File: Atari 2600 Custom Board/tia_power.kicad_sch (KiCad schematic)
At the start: 28 parts, among them J3 USB_C_Receptacle_PowerOnly_6P, Q1 2N3906, SW7 Power, Y1 3.579545 MHz

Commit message: Cleaned up electrical rules violations
Cleaned up electrical rules violations
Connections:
- net CLOCK_IN renamed PHI_2
- net CLOCK_OUT renamed PHI_0
- net ~{RDY} renamed READY
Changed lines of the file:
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@@
 	)
 	(junction
+		(at 76.2 151.13)
+		(diameter 0)
+		(color 0 0 0 0)
+	)
+	(junction
 		(at 228.6 57.15)
 		(diameter 0)
@@
 	)
 	(junction
+		(at 36.83 182.88)
+		(diameter 0)
+		(color 0 0 0 0)
+	)
+	(junction
 		(at 157.48 100.33)
 		(diameter 0)
@@
 	(wire
 		(pts
+			(xy 76.2 151.13) (xy 76.2 157.48)
+		)
+		(stroke
+			(width 0)
+			(type default)
+		)
+	)
+	(wire
+		(pts
 			(xy 55.88 48.26) (xy 55.88 58.42)
 		)
@@
 	(wire
 		(pts
-			(xy 76.2 148.59) (xy 76.2 157.48)
+			(xy 76.2 148.59) (xy 76.2 151.13)
 		)
 		(stroke
@@
 		)
 	)
-	(global_label "CLOCK_OUT"
-		(shape input)
+	(global_label "PHI_0"
+		(shape output)
 		(at 152.4 59.69 180)
 		(fields_autoplaced yes)
@@
 		)
 		(property "Intersheetrefs" "${INTERSHEET_REFS}"
-			(at 138.65 59.69 0)
+			(at 144.0324 59.69 0)
 			(effects
 				(font
@@
 		)
 	)
-	(global_label "CLOCK_IN"
-		(shape output)
+	(global_label "PHI_2"
+		(shape input)
 		(at 204.47 87.63 0)
 		(fields_autoplaced yes)
@@
 		)
 		(property "Intersheetrefs" "${INTERSHEET_REFS}"
-			(at 216.5267 87.63 0)
+			(at 212.8376 87.63 0)
 			(effects
 				(font
@@
 		)
 	)
-	(global_label "~{RDY}"
+	(global_label "READY"
 		(shape output)
 		(at 135.89 57.15 180)
@@
 		)
 		(property "Intersheetrefs" "${INTERSHEET_REFS}"
-			(at 129.2762 57.15 0)
+			(at 127.0386 57.15 0)
 			(effects
 				(font
@@
 	)
 	(symbol
+		(lib_id "power:PWR_FLAG")
+		(at 102.87 152.4 270)
+		(unit 1)
+		(exclude_from_sim no)
+		(in_bom yes)
+		(on_board yes)
+		(dnp no)
+		(fields_autoplaced yes)
+		(property "Reference" "#FLG01"
+			(at 104.775 152.4 0)
+			(effects
+				(font
+					(size 1.27 1.27)
+				)
+				(hide yes)
+			)
+		)
+		(property "Value" "PWR_FLAG"
+			(at 106.68 152.3999 90)
+			(effects
+				(font
+					(size 1.27 1.27)
+				)
+				(justify left)
+			)
+		)
+		(property "Footprint" ""
+			(at 102.87 152.4 0)
+			(effects
+				(font
+					(size 1.27 1.27)
+				)
+				(hide yes)
+			)
+		)
+		(property "Datasheet" "~"
+			(at 102.87 152.4 0)
+			(effects
+				(font
+					(size 1.27 1.27)
+				)
+				(hide yes)
+			)
+		)
+		(property "Description" "Special symbol for telling ERC where power comes from"
+			(at 102.87 152.4 0)
+			(effects
+				(font
+					(size 1.27 1.27)
+				)
+				(hide yes)
+			)
+		)
+		(pin "1"
+		)
+		(instances
+			(project "atari2600"
+				(path "/d26a1e82-f8cb-48a3-8cce-edbb66ba228a/1512de0d-3d07-49f3-86b5-e084744fd125"
+					(reference "#FLG01")
+					(unit 1)
+				)
+			)
+		)
+	)
+	(symbol
 		(lib_id "Device:C")
 		(at 217.17 41.91 180)
@@
 					(unit 1)
 				)
+			)
+		)
+	)
+	(symbol
+		(lib_id "power:PWR_FLAG")
+		(at 76.2 151.13 90)
+		(unit 1)
+		(exclude_from_sim no)
+		(in_bom yes)
+		(on_board yes)
+		(dnp no)
+		(fields_autoplaced yes)
+		(property "Reference" "#FLG02"
+			(at 74.295 151.13 0)
+			(effects
+				(font
+					(size 1.27 1.27)
+				)
+				(hide yes)
+			)
+		)
+		(property "Value" "PWR_FLAG"
+			(at 72.39 151.1299 90)
+			(effects
+				(font
+					(size 1.27 1.27)
+				)
+				(justify left)
+			)
+		)
+		(property "Footprint" ""
+			(at 76.2 151.13 0)
+			(effects
+				(font
+					(size 1.27 1.27)
+				)
+				(hide yes)
+			)
+		)
+		(property "Datasheet" "~"
+			(at 76.2 151.13 0)
+			(effects
+				(font
+					(size 1.27 1.27)
+				)
+				(hide yes)
+			)
+		)
+		(property "Description" "Special symbol for telling ERC where power comes from"
+			(at 76.2 151.13 0)
+			(effects
+				(font
+					(size 1.27 1.27)
+				)
+				(hide yes)
+			)
+		)
+		(pin "1"
+		)
+		(instances
+			(project "atari2600"
+				(path "/d26a1e82-f8cb-48a3-8cce-edbb66ba228a/1512de0d-3d07-49f3-86b5-e084744fd125"
+					(reference "#FLG02")
+					(unit 1)
+				)
+			)
+		)
+	)
+	(symbol
+		(lib_id "power:PWR_FLAG")
+		(at 36.83 182.88 270)
+		(unit 1)
+		(exclude_from_sim no)
+		(in_bom yes)
+		(on_board yes)
+		(dnp no)
+		(fields_autoplaced yes)
+		(property "Reference" "#FLG03"
+			(at 38.735 182.88 0)
+			(effects
+				(font
+					(size 1.27 1.27)
+				)
+				(hide yes)
+			)
+		)
+		(property "Value" "PWR_FLAG"
+			(at 40.64 182.8799 90)
+			(effects
+				(font
+					(size 1.27 1.27)
+				)
+				(justify left)
+			)
+		)
+		(property "Footprint" ""
+			(at 36.83 182.88 0)
+			(effects
+				(font
+					(size 1.27 1.27)
+				)
+				(hide yes)
+			)
+		)
+		(property "Datasheet" "~"
+			(at 36.83 182.88 0)
+			(effects
+				(font
+					(size 1.27 1.27)
+				)
+				(hide yes)
+			)
+		)
+		(property "Description" "Special symbol for telling ERC where power comes from"
+			(at 36.83 182.88 0)
+			(effects
+				(font
+					(size 1.27 1.27)
+				)
+				(hide yes)
+			)
+		)
+		(pin "1"
+		)
+		(instances
+			(project "atari2600"
+				(path "/d26a1e82-f8cb-48a3-8cce-edbb66ba228a/1512de0d-3d07-49f3-86b5-e084744fd125"
+					(reference "#FLG03")
+					(unit 1)
+				)

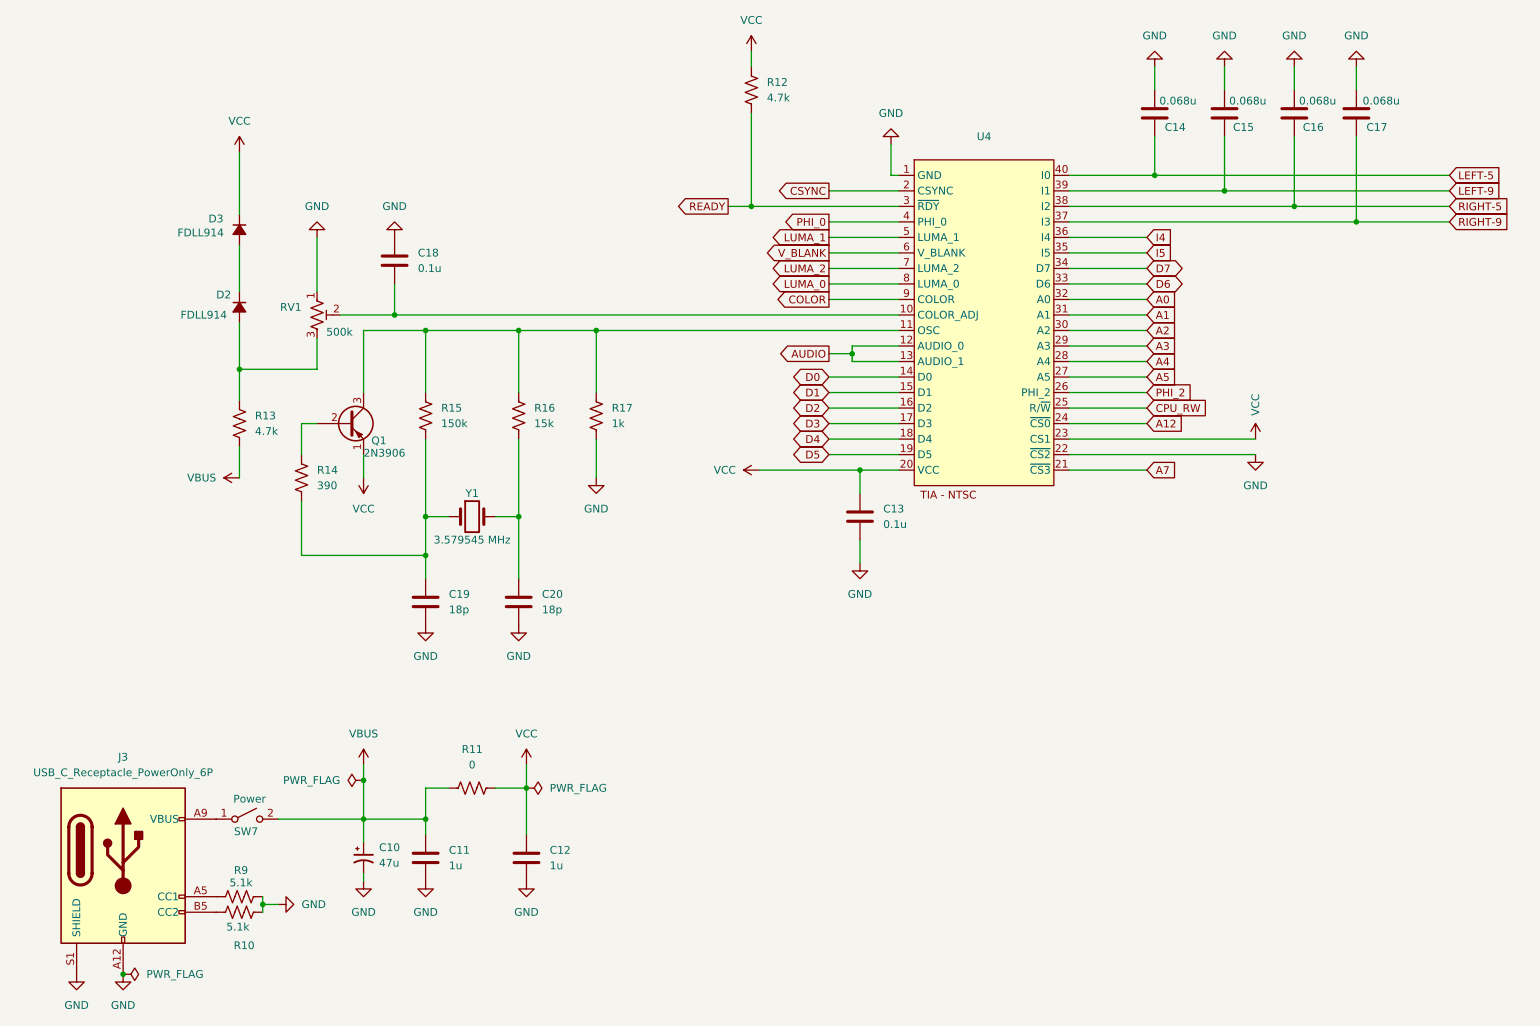
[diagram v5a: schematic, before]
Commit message: Fixed some incorrect values and re-annotated
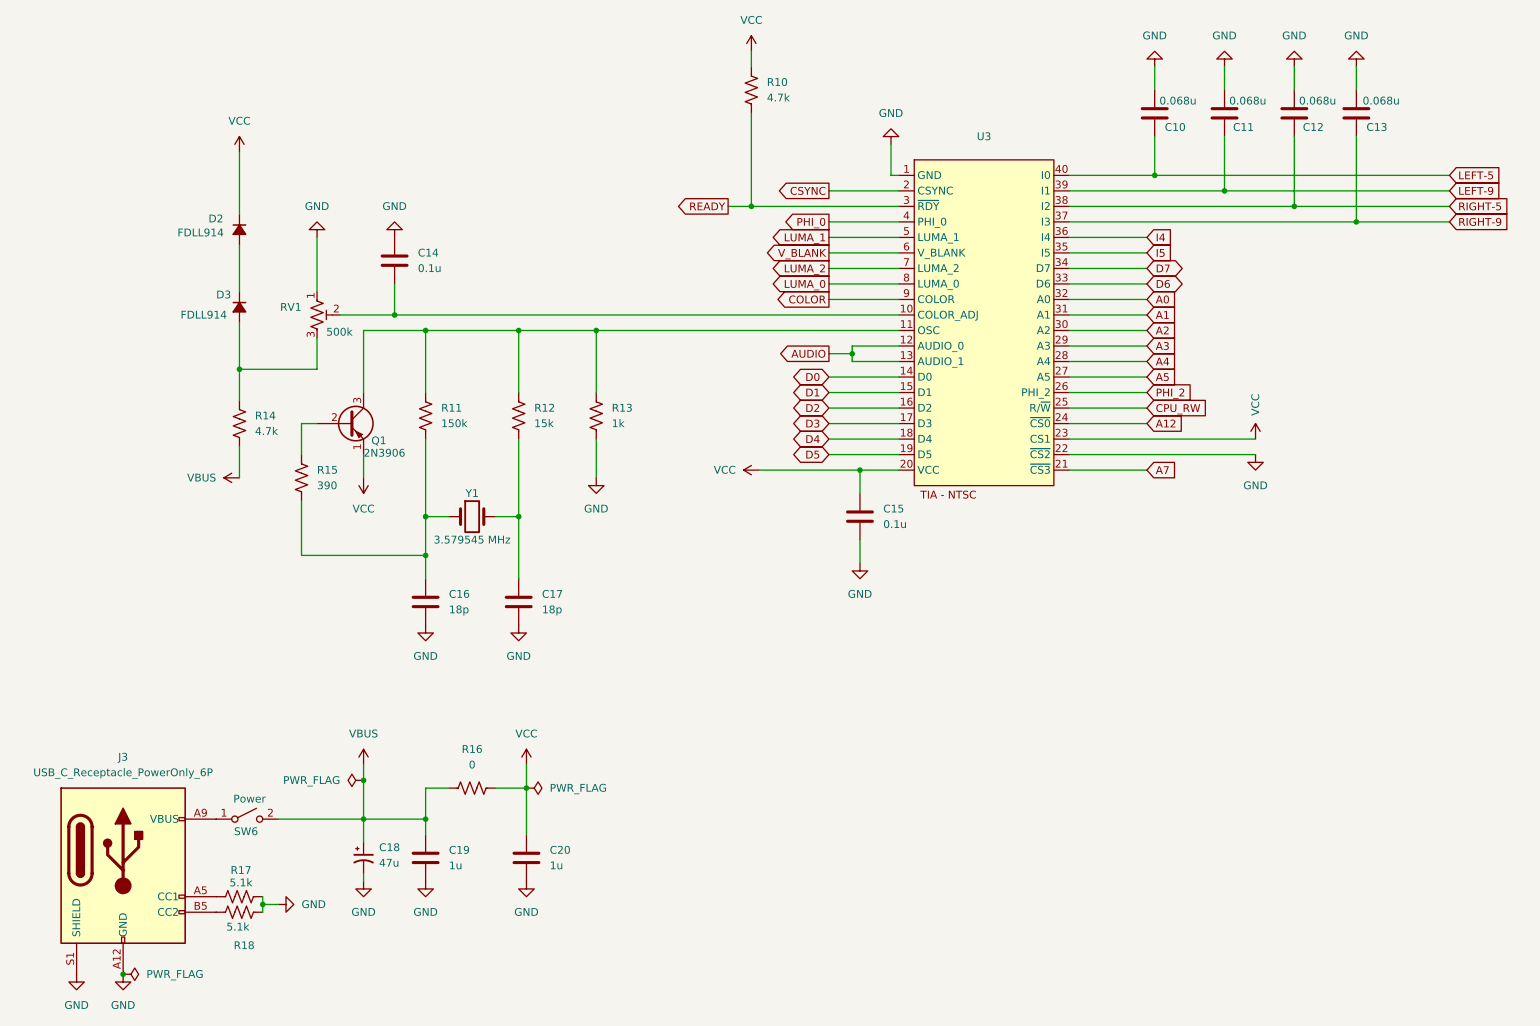
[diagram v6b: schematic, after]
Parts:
- renumbered C14 to C10, C15 to C11, C16 to C12, C17 to C13, C18 to C14, C13 to C15, C19 to C16, C20 to C17, C10 to C18, C11 to C19, C12 to C20, D3 to D2, D2 to D3, R12 to R10, R15 to R11, R16 to R12, R17 to R13, R13 to R14, R14 to R15, R11 to R16, R9 to R17, R10 to R18, SW7 to SW6, U4 to U3

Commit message: assign footprints
assigned most footprints to schematic
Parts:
- C10, C11, C12, C13, C14, C15, C16, C17, C19, C20: footprint (none) -> Capacitor_SMD:C_0805_2012Metric_Pad1.18x1.45mm_HandSolder
- D2, D3: footprint (none) -> Diode_SMD:D_MiniMELF
- R10, R11, R12, R13, R14, R15, R16, R17, R18, RV1: footprint (none) -> Resistor_SMD:R_0805_2012Metric_Pad1.20x1.40mm_HandSolder
- SW6: footprint (none) -> Atari2600_Libary:2600-Toggle-Switch
- U3: footprint (none) -> Package_DIP:DIP-40_W15.24mm_LongPads
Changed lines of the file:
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@@
 			)
 		)
-		(property "Footprint" ""
+		(property "Footprint" "Capacitor_SMD:C_0805_2012Metric_Pad1.18x1.45mm_HandSolder"
 			(at 158.4452 111.76 0)
 			(effects
@@
 			)
 		)
-		(property "Footprint" ""
+		(property "Footprint" "Capacitor_SMD:C_0805_2012Metric_Pad1.18x1.45mm_HandSolder"
 			(at 216.2048 38.1 0)
 			(effects
@@
 			)
 		)
-		(property "Footprint" ""
+		(property "Footprint" "Resistor_SMD:R_0805_2012Metric_Pad1.20x1.40mm_HandSolder"
 			(at 68.58 74.93 0)
 			(effects
@@
 			)
 		)
-		(property "Footprint" ""
+		(property "Footprint" "Package_DIP:DIP-40_W15.24mm_LongPads"
 			(at 166.37 49.53 0)
 			(effects
@@
 			)
 		)
-		(property "Footprint" ""
+		(property "Footprint" "Resistor_SMD:R_0805_2012Metric_Pad1.20x1.40mm_HandSolder"
 			(at 56.134 169.164 90)
 			(effects
@@
 			)
 		)
-		(property "Footprint" ""
+		(property "Footprint" "Capacitor_SMD:C_0805_2012Metric_Pad1.18x1.45mm_HandSolder"
 			(at 237.7948 38.1 0)
 			(effects
@@
 			)
 		)
-		(property "Footprint" ""
+		(property "Footprint" "Capacitor_SMD:C_0805_2012Metric_Pad1.18x1.45mm_HandSolder"
 			(at 204.7748 38.1 0)
 			(effects
@@
 			)
 		)
-		(property "Footprint" ""
+		(property "Footprint" "Capacitor_SMD:C_0805_2012Metric_Pad1.18x1.45mm_HandSolder"
 			(at 82.2452 69.85 0)
 			(effects
@@
 			)
 		)
-		(property "Footprint" ""
+		(property "Footprint" "Diode_SMD:D_MiniMELF"
 			(at 55.88 60.96 90)
 			(effects
@@
 			)
 		)
-		(property "Footprint" ""
+		(property "Footprint" "Capacitor_SMD:C_0805_2012Metric_Pad1.18x1.45mm_HandSolder"
 			(at 103.8352 167.64 0)
 			(effects
@@
 			)
 		)
-		(property "Footprint" ""
+		(property "Footprint" "Resistor_SMD:R_0805_2012Metric_Pad1.20x1.40mm_HandSolder"
 			(at 94.234 151.384 90)
 			(effects
@@
 			)
 		)
-		(property "Footprint" ""
+		(property "Footprint" "Resistor_SMD:R_0805_2012Metric_Pad1.20x1.40mm_HandSolder"
 			(at 65.024 101.346 90)
 			(effects
@@
 			)
 		)
-		(property "Footprint" ""
+		(property "Footprint" "Resistor_SMD:R_0805_2012Metric_Pad1.20x1.40mm_HandSolder"
 			(at 140.716 38.354 90)
 			(effects
@@
 			)
 		)
-		(property "Footprint" ""
+		(property "Footprint" "Diode_SMD:D_MiniMELF"
 			(at 55.88 73.66 90)
 			(effects
@@
 			)
 		)
-		(property "Footprint" ""
+		(property "Footprint" "Capacitor_SMD:C_0805_2012Metric_Pad1.18x1.45mm_HandSolder"
 			(at 227.6348 38.1 0)
 			(effects
@@
 			)
 		)
-		(property "Footprint" ""
+		(property "Footprint" "Resistor_SMD:R_0805_2012Metric_Pad1.20x1.40mm_HandSolder"
 			(at 55.626 173.736 90)
 			(effects
@@
 			)
 		)
-		(property "Footprint" ""
+		(property "Footprint" "Capacitor_SMD:C_0805_2012Metric_Pad1.18x1.45mm_HandSolder"
 			(at 87.3252 125.73 0)
 			(effects
@@
 			)
 		)
-		(property "Footprint" ""
+		(property "Footprint" "Resistor_SMD:R_0805_2012Metric_Pad1.20x1.40mm_HandSolder"
 			(at 85.344 91.186 90)
 			(effects
@@
 			)
 		)
-		(property "Footprint" ""
+		(property "Footprint" "Resistor_SMD:R_0805_2012Metric_Pad1.20x1.40mm_HandSolder"
 			(at 113.284 91.186 90)
 			(effects
@@
 			)
 		)
-		(property "Footprint" ""
+		(property "Footprint" "Capacitor_SMD:C_0805_2012Metric_Pad1.18x1.45mm_HandSolder"
 			(at 102.5652 125.73 0)
 			(effects
@@
 			)
 		)
-		(property "Footprint" ""
+		(property "Footprint" "Capacitor_SMD:C_0805_2012Metric_Pad1.18x1.45mm_HandSolder"
 			(at 87.3252 167.64 0)
 			(effects
@@
 			)
 		)
-		(property "Footprint" ""
+		(property "Footprint" "Atari2600_Libary:2600-Toggle-Switch"
 			(at 57.15 157.48 0)
 			(effects
@@
 			)
 		)
-		(property "Footprint" ""
+		(property "Footprint" "Resistor_SMD:R_0805_2012Metric_Pad1.20x1.40mm_HandSolder"
 			(at 54.864 92.456 90)
 			(effects
@@
 			)
 		)
-		(property "Footprint" ""
+		(property "Footprint" "Resistor_SMD:R_0805_2012Metric_Pad1.20x1.40mm_HandSolder"
 			(at 100.584 91.186 90)
 			(effects

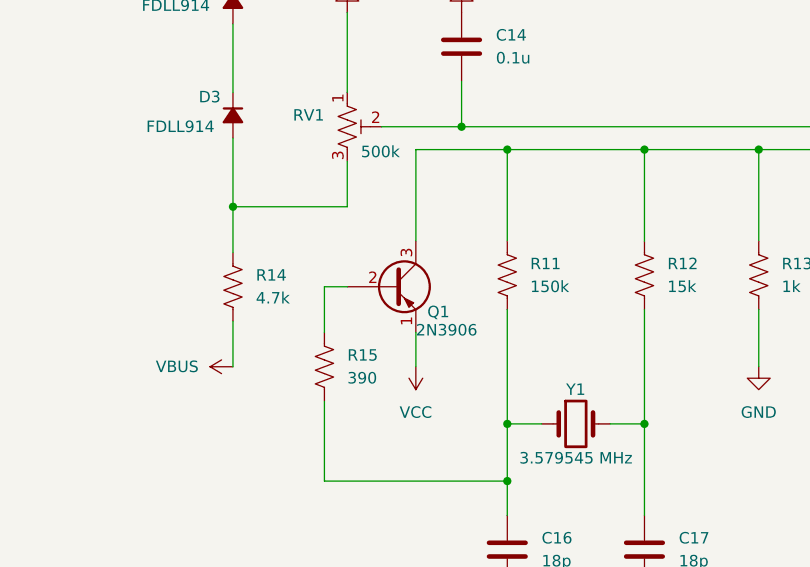
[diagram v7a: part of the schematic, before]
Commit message: Fixed incorrect 3906 transistor symbol pinout
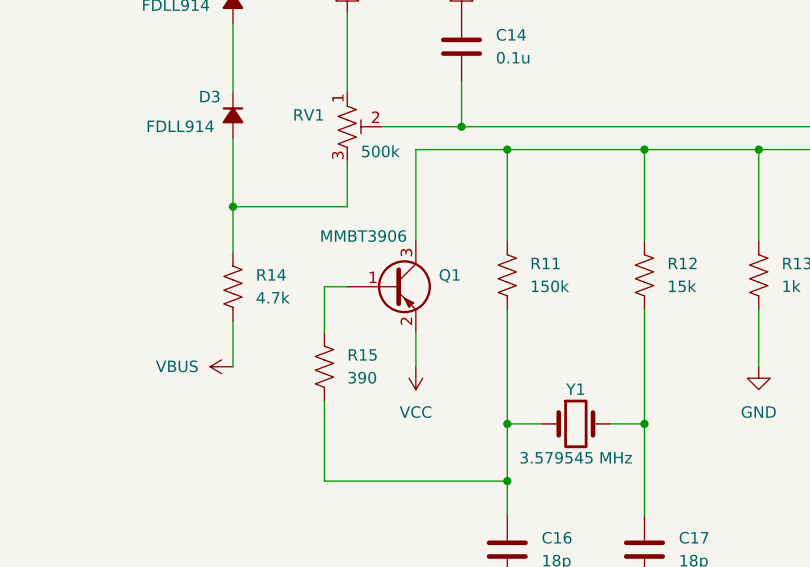
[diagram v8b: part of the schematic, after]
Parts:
- removed Q1: 2N3906, Package_TO_SOT_THT:TO-92_Inline, symbol Transistor_BJT:2N3906
- added Q1: MMBT3906, Package_TO_SOT_SMD:SOT-23, symbol Transistor_BJT:MMBT3906
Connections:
- net VCC: now also Q1.2 (E)
- net at R11.2, R12.2, R13.2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: now also Q1.3 (C)
- net at R15.2: now also Q1.1 (B)
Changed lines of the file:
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@@
+	)
+	(symbol
+		(lib_id "Transistor_BJT:MMBT3906")
+		(at 73.66 92.71 0)
+		(unit 1)
+		(exclude_from_sim no)
+		(in_bom yes)
+		(on_board yes)
+		(dnp no)
+		(property "Reference" "Q1"
+			(at 78.74 91.4399 0)
+			(effects
+				(font
+					(size 1.27 1.27)
+				)
+				(justify left)
+			)
+		)
+		(property "Value" "MMBT3906"
+			(at 65.532 87.122 0)
+			(effects
+				(font
+					(size 1.27 1.27)
+				)
+				(justify left)
+			)
+		)
+		(property "Footprint" "Package_TO_SOT_SMD:SOT-23"
+			(at 78.74 94.615 0)
+			(effects
+				(font
+					(size 1.27 1.27)
+					(italic yes)
+				)
+				(justify left)
+				(hide yes)
+			)
+		)
+		(property "Datasheet" "https://www.onsemi.com/pdf/datasheet/pzt3906-d.pdf"
+			(at 73.66 92.71 0)
+			(effects
+				(font
+					(size 1.27 1.27)
+				)
+				(justify left)
+				(hide yes)
+			)
+		)
+		(property "Description" "-0.2A Ic, -40V Vce, Small Signal PNP Transistor, SOT-23"
+			(at 73.66 92.71 0)
+			(effects
+				(font
+					(size 1.27 1.27)
+				)
+				(hide yes)
+			)
+		)
+		(pin "1"
+		)
+		(pin "3"
+		)
+		(pin "2"
+		)
+		(instances
+			(project "atari2600"
+				(path "/d26a1e82-f8cb-48a3-8cce-edbb66ba228a/1512de0d-3d07-49f3-86b5-e084744fd125"
+					(reference "Q1")
+					(unit 1)
+				)
+			)
+		)
 	)
 	(symbol
@@
 					(unit 1)
 				)
-			)
-		)
-	)
-	(symbol
-		(lib_id "Transistor_BJT:2N3906")
-		(at 73.66 92.71 0)
-		(unit 1)
-		(exclude_from_sim no)
-		(in_bom yes)
-		(on_board yes)
-		(dnp no)
-		(property "Reference" "Q1"
-			(at 77.47 95.504 0)
-			(effects
-				(font
-					(size 1.27 1.27)
-				)
-				(justify left)
-			)
-		)
-		(property "Value" "2N3906"
-			(at 76.2 97.536 0)
-			(effects
-				(font
-					(size 1.27 1.27)
-				)
-				(justify left)
-			)
-		)
-		(property "Footprint" "Package_TO_SOT_THT:TO-92_Inline"
-			(at 78.74 94.615 0)
-			(effects
-				(font
-					(size 1.27 1.27)
-					(italic yes)
-				)
-				(justify left)
-				(hide yes)
-			)
-		)
-		(property "Datasheet" "https://www.onsemi.com/pub/Collateral/2N3906-D.PDF"
-			(at 73.66 92.71 0)
-			(effects
-				(font
-					(size 1.27 1.27)
-				)
-				(justify left)
-				(hide yes)
-			)
-		)
-		(property "Description" "-0.2A Ic, -40V Vce, Small Signal PNP Transistor, TO-92"
-			(at 73.66 92.71 0)
-			(effects
-				(font
-					(size 1.27 1.27)
-				)
-				(hide yes)
-			)
-		)
-		(pin "2"
-		)
-		(pin "3"
-		)
-		(pin "1"
-		)
-		(instances
-			(project "atari2600"
-				(path "/d26a1e82-f8cb-48a3-8cce-edbb66ba228a/1512de0d-3d07-49f3-86b5-e084744fd125"
-					(reference "Q1")
-					(unit 1)
-				)
